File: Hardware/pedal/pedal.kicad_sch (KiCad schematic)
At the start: 35 parts, among them J101 USB_C_Receptacle_USB2.0_16P, J102 Barrel_Jack_Switch, J103 AudioJack3_SwitchTR, SW101 SW_SPST, SW102 SW_SPST, SW103 RotaryEncoder_Switch_MP, U101 USBLC6-2P6, U102 TPS62153, U103 TLV76733DRVx

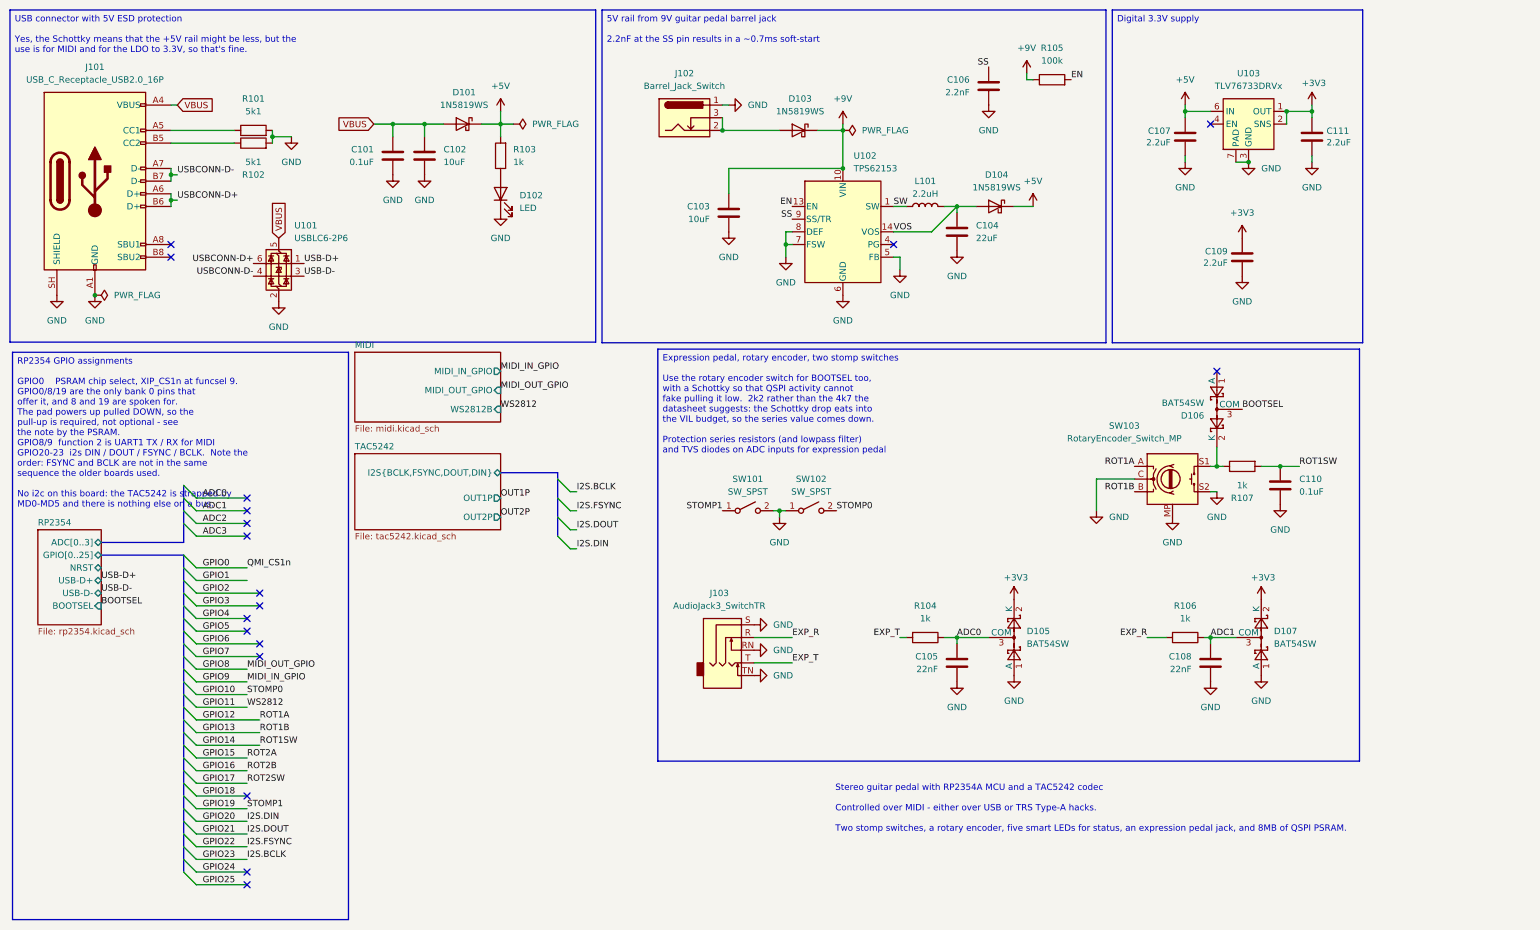
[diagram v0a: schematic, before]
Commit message: Start re-doing the 'pedal' part without any actual audio processing
The 'minimal' board is what I think is the right way to go, and works
very well.  Being able to use WebMIDI over BLE just means that it's a
lot more convenient to use from a phone or a computer.

But as an actual *pedal* that minimal board isn't great.  It
intentionally has no actual physical controls, and since it's USB-C only
it doesn't work well on a traditional pedal board anyway.

But the plan was always to make things a bit more modular.  This is the
beginnings of that.  The non-minimal 'pedal' design has stomp switches
and hardware MIDI connectors and an expression pedal jack, and those all
worked fine.  It also has the traditional guitar pedal 9V DC jack.

So this just removes the actual audio side of it and only leaves that
cheap and useful rp2354 as the control piece and USB controller (it
never grew BLE support).  But now the main use of USB is as a USB
_host_, and as a way to power the minimal board.  It still presents as a
USB device for programming purposes, but that's now _purely_ for
programming.

[ Side note: the USB CC lines still claim it's acting as a USB device -
  exactly for that programming case. The minimal pedal doesn't care. All
  it wants is USB data lines and VBUS, so that "USB host" side is a bit
  dodgy from a USB standard side, but I can't find it in myself to
  really care. This isn't designed as some kind of generic USB host,
  it's designed explicitly as just a host for the minimal pedal design ]

So the usage scenario is that you connect your 9V guitar power to this
pedal, and use it as a pedal: it has the stomp switch and all controls
on it.  Then you snake the USB-C cable to the minimal box, which is
where you connect the audio to, and where all audio processing takes
place.

The pedal still has a TRS 6.35mm jack and two TRS 3.5mm jacks, but they
are purely for the remove switch (or expression pedal) and the Type-A
TRS MIDI connections.  No actual audio anywhere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
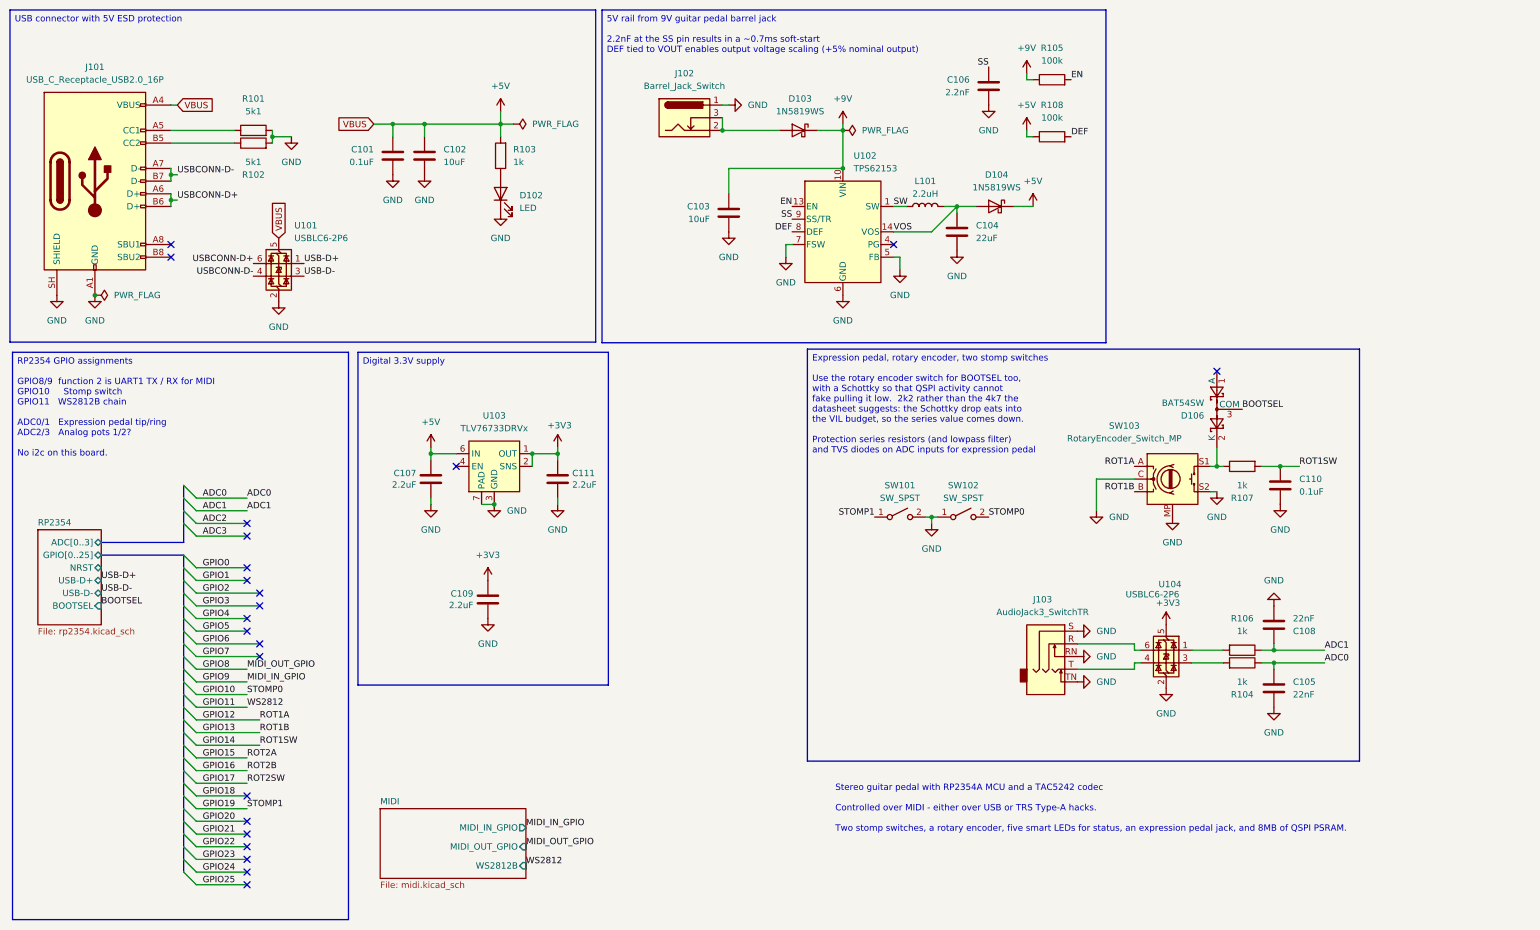
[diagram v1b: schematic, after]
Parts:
- removed D101: 1N5819WS, Diode_SMD:D_SOD-323, symbol Device:D_Schottky
- removed D105, D107: BAT54SW, Package_TO_SOT_SMD:SOT-323_SC-70, symbol Diode:BAT54SW
- added R108: 100k, Resistor_SMD:R_0402_1005Metric, symbol Device:R
- added U104: USBLC6-2P6, Package_TO_SOT_SMD:SOT-666, symbol Power_Protection:USBLC6-2P6
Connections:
- net VBUS is gone; now on net +5V: C101.2, C102.1, J101.A4 (VBUS), J101.A9 (VBUS), J101.B4 (VBUS), J101.B9 (VBUS), U101.5 (VBUS)
- net +3V3: now also U104.5 (VBUS)
- net +5V: now also R108.1
- net GND: now also U104.2 (GND); no longer U102.8 (DEF)
- net EXP_R: no longer names the net of R106.2
- net EXP_R: now also U104.1 (I/O1); no longer J103.R
- net EXP_T: no longer names the net of J103.T
- net EXP_T: now also U104.4 (I/O2); no longer R104.2
- new net: J103.R, U104.6 (I/O1)
- new net: R104.2, U104.3 (I/O2)
- new net DEF: R108.2, U102.8 (DEF)
- no-connect marks 18 -> 22
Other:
- removed sheet TAC5242
- moved on the sheet: C105, C107, C108, C109, C111, J103, R104, R106, SW101, SW102, U103
